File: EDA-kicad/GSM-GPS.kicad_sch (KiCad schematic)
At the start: 3 parts, among them J2 SIM-G85D1160022HHR, U1 GSM-GPS-EC25VFA-512-STD, U2 EG25GGC-128-SGNS

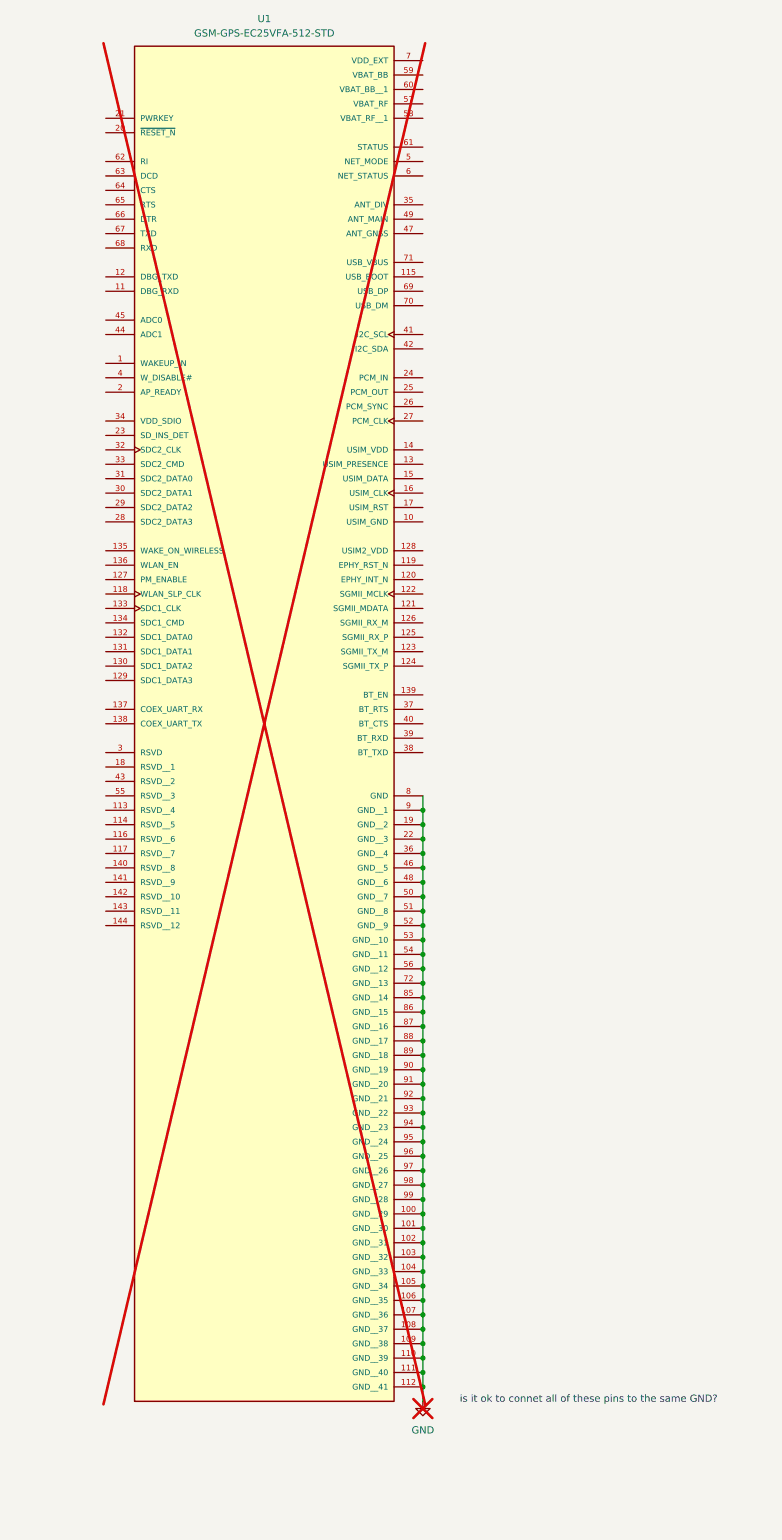
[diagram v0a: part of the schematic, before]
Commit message: change netflaf for microphone switch to be 1V8 instead of 3V3B, GPS/GSM symbol
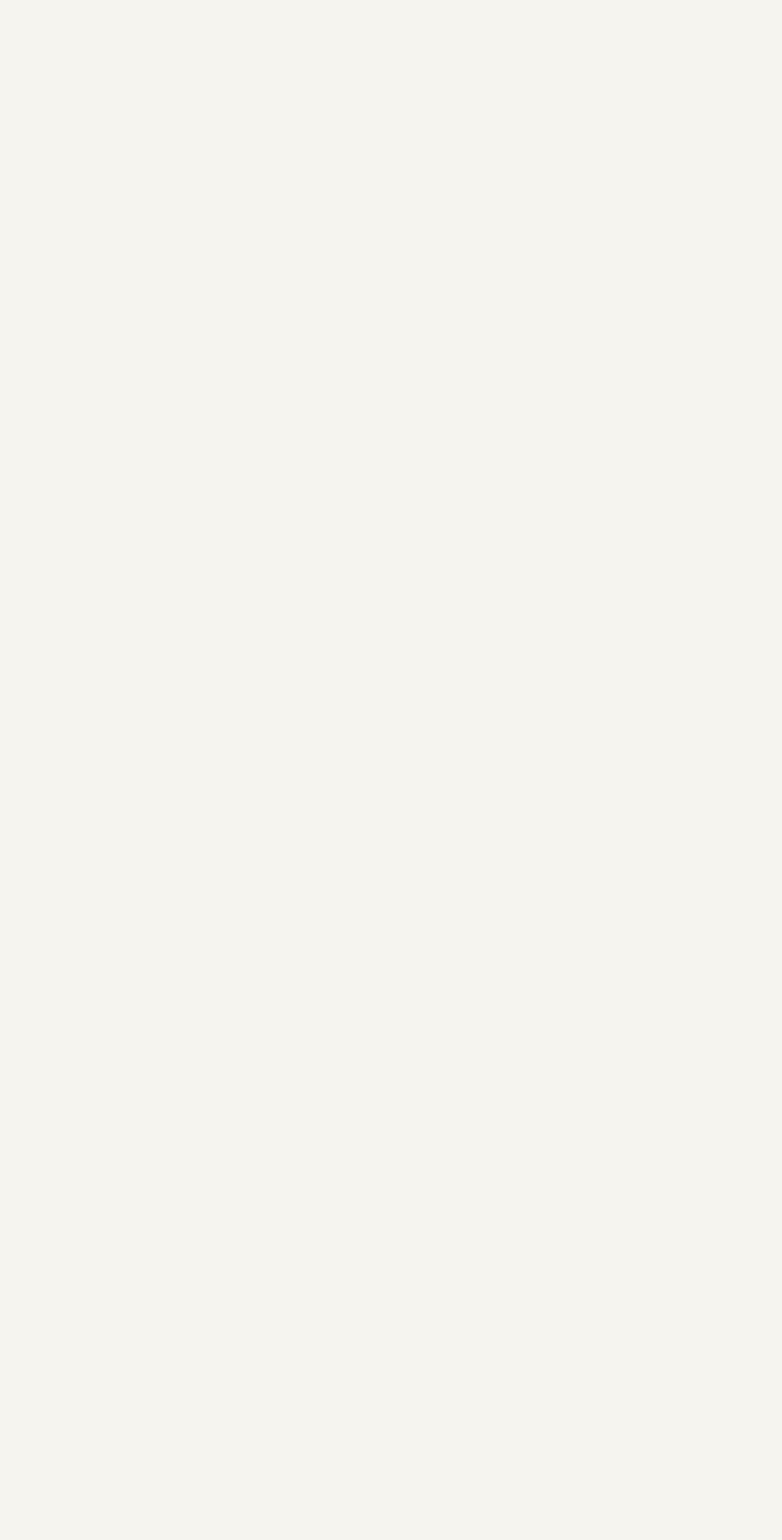
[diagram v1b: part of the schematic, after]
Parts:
- removed U1: GSM-GPS-EC25VFA-512-STD, SPIRIT-footprints:GSM-GPS-XCVR_EC25VFA-512-STD, symbol SPIRIT-components:GSM-GPS-EC25VFA-512-STD
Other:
- note removed: "is it ok to connet all of these pins to the same GND?"

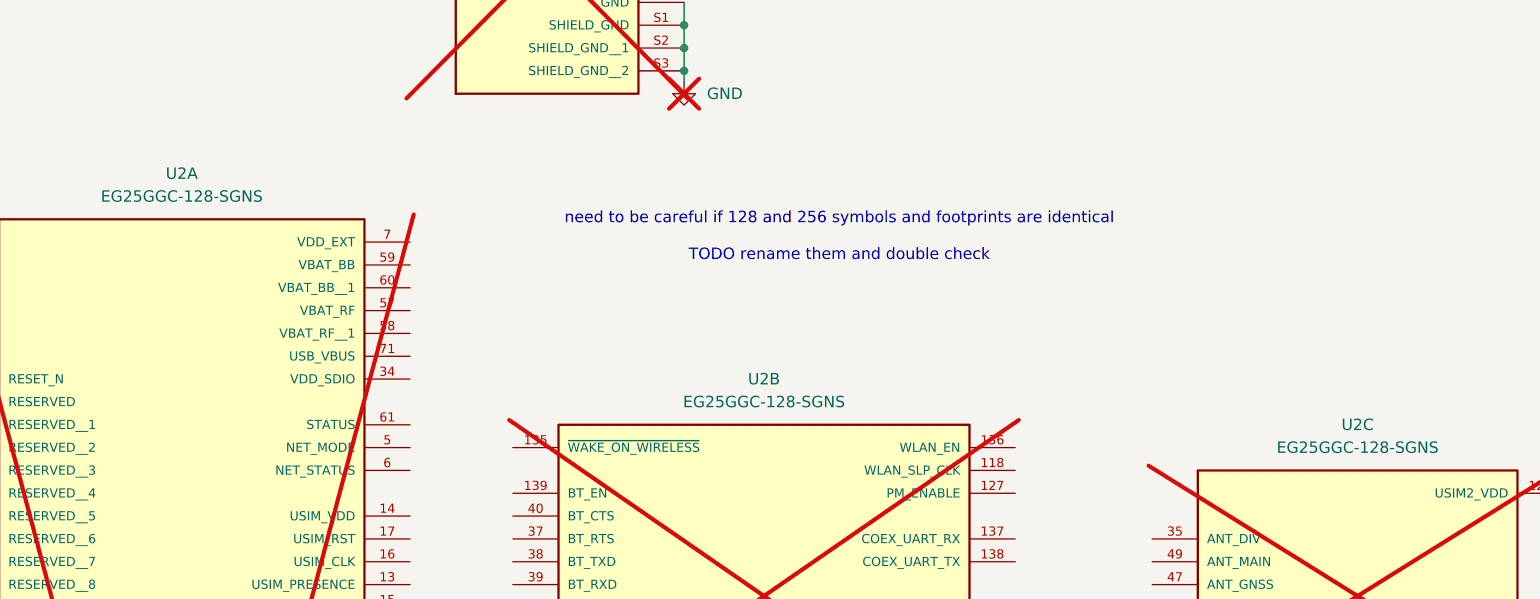
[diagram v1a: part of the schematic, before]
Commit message: reannotate entire schematic
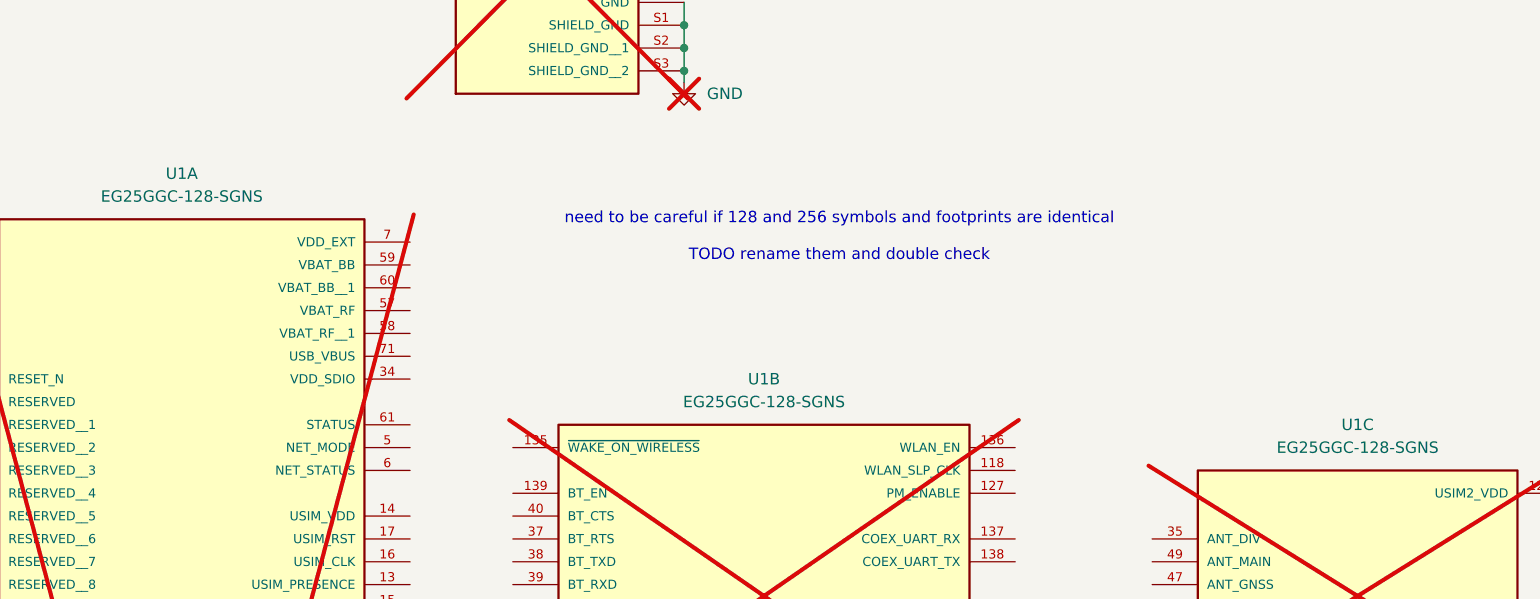
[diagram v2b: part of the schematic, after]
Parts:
- renumbered U2 to U1
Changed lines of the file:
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@@
 		(dnp yes)
 		(fields_autoplaced yes)
-		(property "Reference" "U2"
+		(property "Reference" "U1"
 			(at 226.06 105.41 0)
 			(effects
@@
 			(project ""
 				(path "/28c5e4fe-1ec7-4477-97f0-d2ec1401fad5/1297454b-0b1d-459e-9de1-2b16d7982efe"
-					(reference "U2")
+					(reference "U1")
 					(unit 3)
 				)
@@
 		(dnp yes)
 		(fields_autoplaced yes)
-		(property "Reference" "U2"
+		(property "Reference" "U1"
 			(at 95.25 77.47 0)
 			(effects
@@
 			(project ""
 				(path "/28c5e4fe-1ec7-4477-97f0-d2ec1401fad5/1297454b-0b1d-459e-9de1-2b16d7982efe"
-					(reference "U2")
+					(reference "U1")
 					(unit 1)
 				)
@@
 		(dnp yes)
 		(fields_autoplaced yes)
-		(property "Reference" "U2"
+		(property "Reference" "U1"
 			(at 160.02 100.33 0)
 			(effects
@@
 			(project ""
 				(path "/28c5e4fe-1ec7-4477-97f0-d2ec1401fad5/1297454b-0b1d-459e-9de1-2b16d7982efe"
-					(reference "U2")
+					(reference "U1")
 					(unit 2)
 				)
